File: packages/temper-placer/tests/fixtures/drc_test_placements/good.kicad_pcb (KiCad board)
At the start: 2 copper layers, 50 x 30 mm, 4 parts, among them U1 LM358

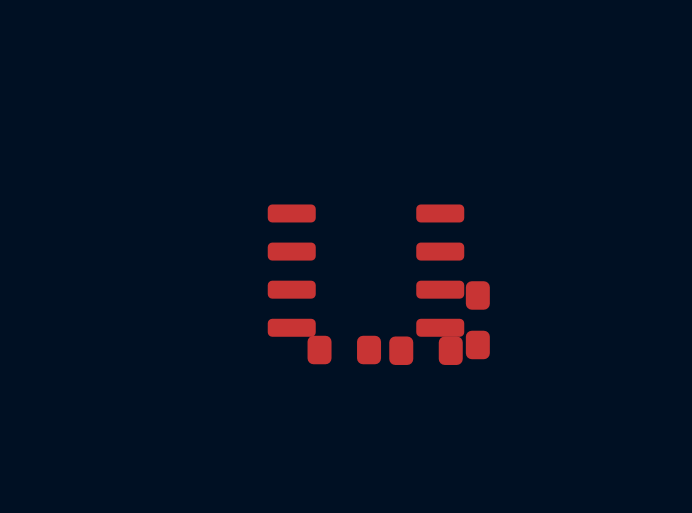
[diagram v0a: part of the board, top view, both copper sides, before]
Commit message: feat(placer): NSGA-II, Crawler, NetCentroidLoss, and structural refinements
- Implemented NSGA-II multi-objective optimization
- Added PcbCrawler for GitHub data collection
- Implemented NetCentroidAttractionLoss
- Unified optimization pipeline with explicit phases
- Fixed ruff linting errors and optimized imports
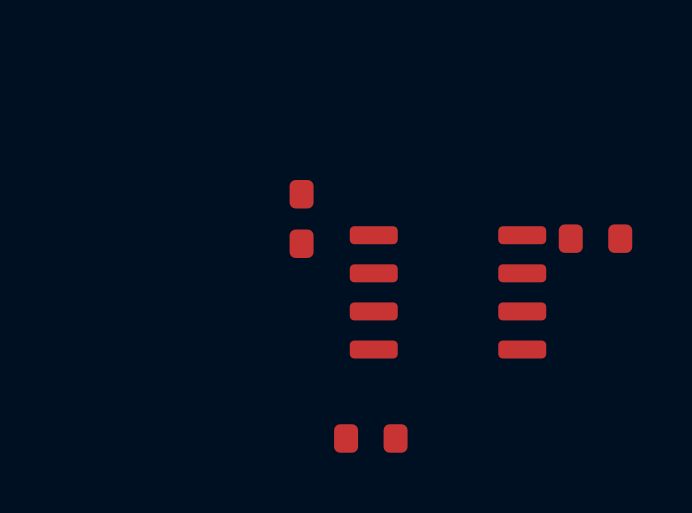
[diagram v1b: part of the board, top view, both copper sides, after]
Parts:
- moved C1 4.77 mm to (212.0, 151.6), turned to 0 degrees
- moved R1 4.59 mm to (202.2, 151.0), turned to 90 degrees
- moved R2 3.46 mm to (204.5, 158.3), turned to 0 degrees
- moved U1 2.83 mm to (207.1, 153.4), turned to 0 degrees
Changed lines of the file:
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@@
   (net 4 "SIG2")
   (footprint "Resistor_SMD:R_0603_1608Metric" (layer "F.Cu")
-    (at 203.62545238394125 155.3403145720717 0.0)
+    (at 202.20253642997244 150.9729914997215 90.0)
     (property "Reference" "R1")
     (property "Value" "10k")
@@
   )
   (footprint "Resistor_SMD:R_0603_1608Metric" (layer "F.Cu")
-    (at 206.34986399963225 155.36405016889017 180.0)
+    (at 204.51042163898182 158.2889805962489 0.0)
     (property "Reference" "R2")
     (property "Value" "4.7k")
@@
   )
   (footprint "Capacitor_SMD:C_0603_1608Metric" (layer "F.Cu")
-    (at 208.07757608066288 154.34710723176667 90.0)
+    (at 211.99947175406612 151.6278695582765 0.0)
     (property "Reference" "C1")
     (property "Value" "100nF")
@@
   )
   (footprint "Package_SO:SOIC-8_3.9x4.9mm_P1.27mm" (layer "F.Cu")
-    (at 204.34950811745597 152.69385059944486 180.0)
+    (at 207.08303911998922 153.41879931193108 0.0)
     (property "Reference" "U1")
     (property "Value" "LM358")

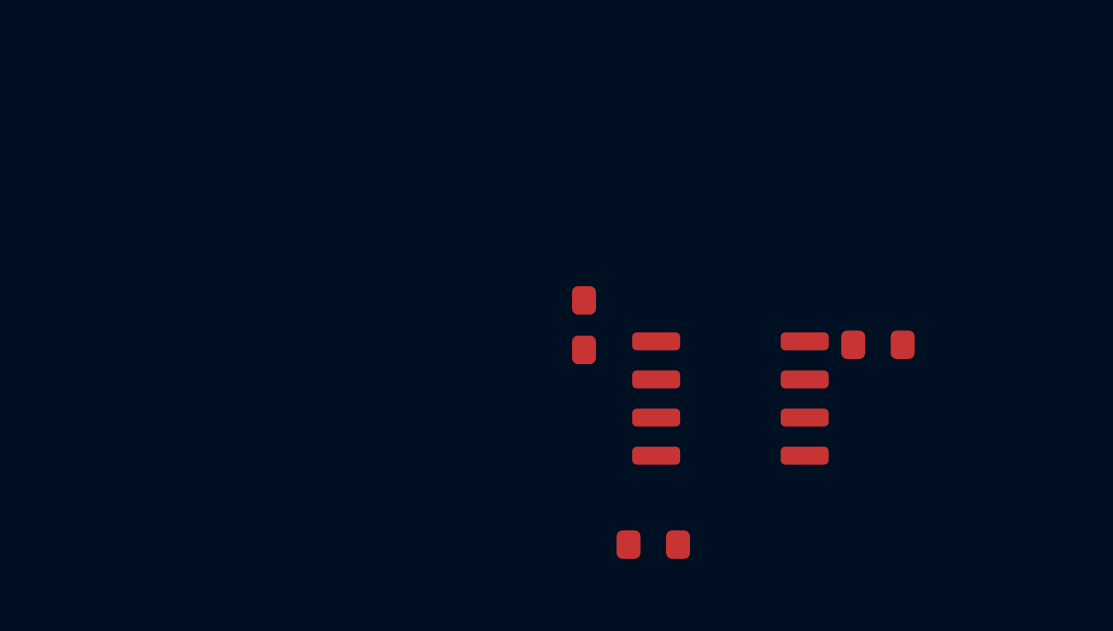
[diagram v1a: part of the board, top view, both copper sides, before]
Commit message: feat(placer): vectorize GroundCrossingLoss and add star-ground awareness
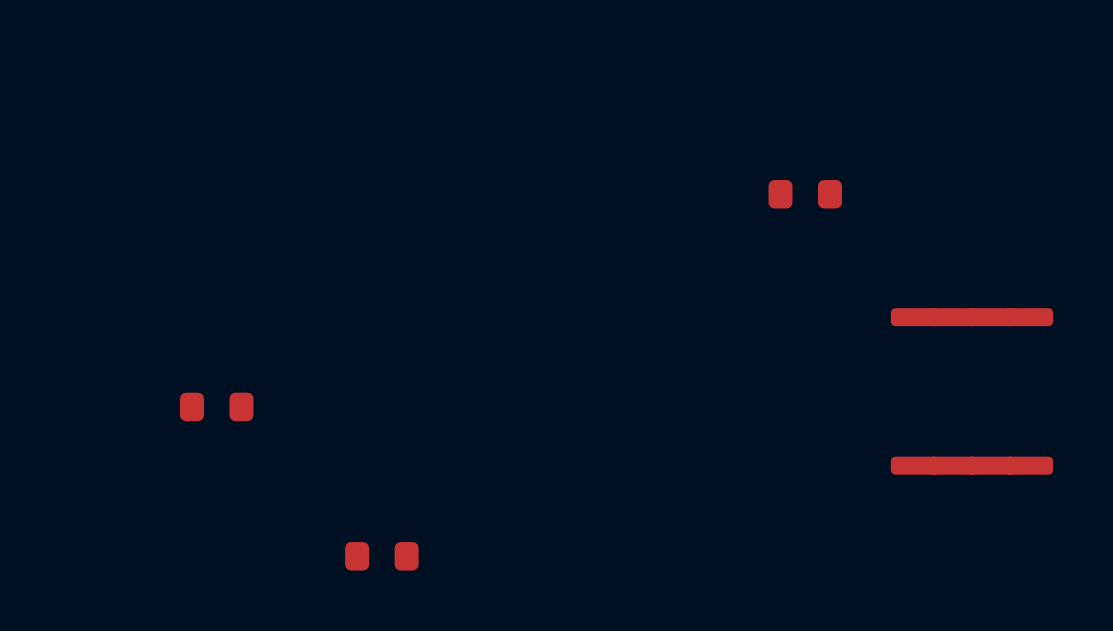
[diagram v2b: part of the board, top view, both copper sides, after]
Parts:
- moved R1 12.5 mm to (190.0, 153.7), turned to 180 degrees
- moved R2 9.05 mm to (195.5, 158.7), turned to 180 degrees
- moved U1 8.06 mm to (215.1, 153.2), turned to 90 degrees
- moved C1 5.57 mm to (209.6, 146.6), turned to 180 degrees
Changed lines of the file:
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@@
   (net 4 "SIG2")
   (footprint "Resistor_SMD:R_0603_1608Metric" (layer "F.Cu")
-    (at 202.20253642997244 150.9729914997215 90.0)
+    (at 189.96026317155744 153.70019848975193 180.0)
     (property "Reference" "R1")
     (property "Value" "10k")
@@
   )
   (footprint "Resistor_SMD:R_0603_1608Metric" (layer "F.Cu")
-    (at 204.51042163898182 158.2889805962489 0.0)
+    (at 195.4638047716711 158.67849316057936 180.0)
     (property "Reference" "R2")
     (property "Value" "4.7k")
@@
   )
   (footprint "Capacitor_SMD:C_0603_1608Metric" (layer "F.Cu")
-    (at 211.99947175406612 151.6278695582765 0.0)
+    (at 209.57740181160239 146.6107337484442 180.0)
     (property "Reference" "C1")
     (property "Value" "100nF")
@@
   )
   (footprint "Package_SO:SOIC-8_3.9x4.9mm_P1.27mm" (layer "F.Cu")
-    (at 207.08303911998922 153.41879931193108 0.0)
+    (at 215.13573126750356 153.18306676152255 90.0)
     (property "Reference" "U1")
     (property "Value" "LM358")

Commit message: feat: Consolidate implementations for Manufacturing, Star Point, and Analysis tasks
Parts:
- turned C1 to 270 degrees
- turned R1 to 270 degrees
- turned R2 to 270 degrees
- turned U1 to 270 degrees
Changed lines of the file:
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@@
   (net 4 "SIG2")
   (footprint "Resistor_SMD:R_0603_1608Metric" (layer "F.Cu")
-    (at 189.96026317155744 153.70019848975193 180.0)
+    (at 189.96026317155744 153.70019848975193 270.0)
     (property "Reference" "R1")
     (property "Value" "10k")
@@
   )
   (footprint "Resistor_SMD:R_0603_1608Metric" (layer "F.Cu")
-    (at 195.4638047716711 158.67849316057936 180.0)
+    (at 195.4638047716711 158.67849316057936 270.0)
     (property "Reference" "R2")
     (property "Value" "4.7k")
@@
   )
   (footprint "Capacitor_SMD:C_0603_1608Metric" (layer "F.Cu")
-    (at 209.57740181160239 146.6107337484442 180.0)
+    (at 209.57740181160239 146.6107337484442 270.0)
     (property "Reference" "C1")
     (property "Value" "100nF")
@@
   )
   (footprint "Package_SO:SOIC-8_3.9x4.9mm_P1.27mm" (layer "F.Cu")
-    (at 215.13573126750356 153.18306676152255 90.0)
+    (at 215.13573126750356 153.18306676152255 270.0)
     (property "Reference" "U1")
     (property "Value" "LM358")

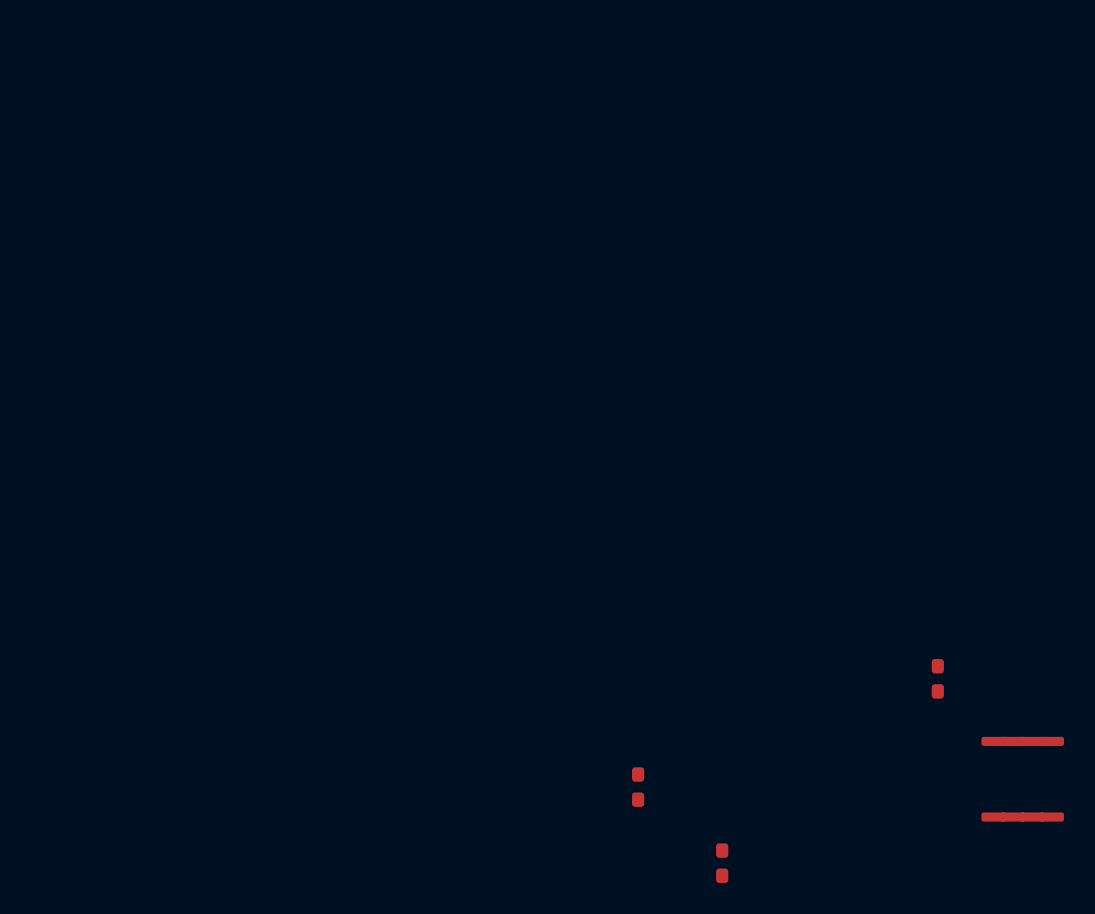
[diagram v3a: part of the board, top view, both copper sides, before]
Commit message: fix(placer): resolve all critical optimizer bugs in temper-p11g
- Fixed JAX array len() TypeErrors by using .shape[0]\n- Corrected BoundaryLoss to use absolute coordinates for non-zero origin boards\n- Implemented hard position and virtual node clamping in training loop\n- Fixed TypeError in force_directed.py random_init call\n- Cleaned up outdated Board/Component signatures in tests
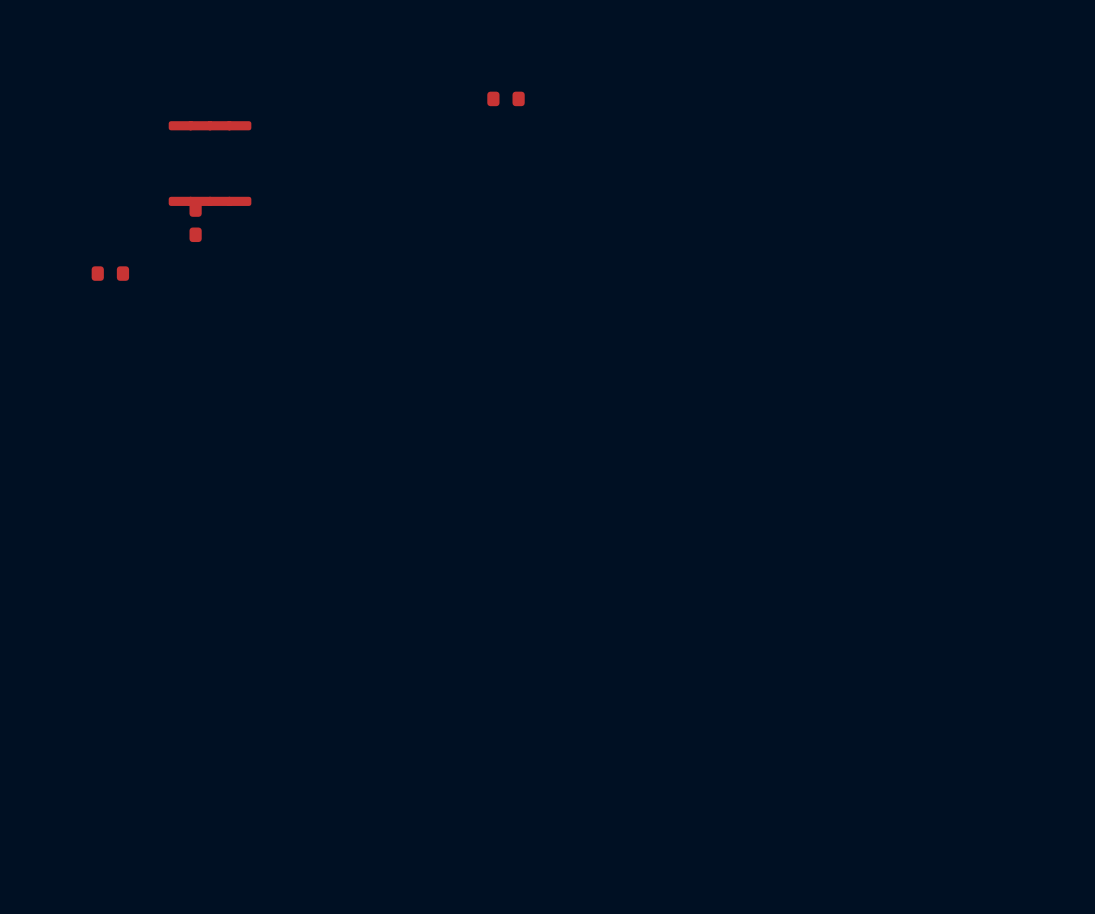
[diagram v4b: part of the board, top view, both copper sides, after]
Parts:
- moved U1 66.7 mm to (161.9, 112.9)
- moved R2 54.3 mm to (161.0, 116.7), turned to 90 degrees
- moved R1 48.2 mm to (155.4, 120.1), turned to 180 degrees
- moved C1 47.3 mm to (181.3, 108.7), turned to 0 degrees
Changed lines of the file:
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@@
   (net 4 "SIG2")
   (footprint "Resistor_SMD:R_0603_1608Metric" (layer "F.Cu")
-    (at 189.96026317155744 153.70019848975193 270.0)
+    (at 155.41230672692365 120.08329051513866 180.0)
     (property "Reference" "R1")
     (property "Value" "10k")
@@
   )
   (footprint "Resistor_SMD:R_0603_1608Metric" (layer "F.Cu")
-    (at 195.4638047716711 158.67849316057936 270.0)
+    (at 160.99183216974504 116.71895349326667 90.0)
     (property "Reference" "R2")
     (property "Value" "4.7k")
@@
   )
   (footprint "Capacitor_SMD:C_0603_1608Metric" (layer "F.Cu")
-    (at 209.57740181160239 146.6107337484442 270.0)
+    (at 181.3108780610052 108.65010905005963 0.0)
     (property "Reference" "C1")
     (property "Value" "100nF")
@@
   )
   (footprint "Package_SO:SOIC-8_3.9x4.9mm_P1.27mm" (layer "F.Cu")
-    (at 215.13573126750356 153.18306676152255 270.0)
+    (at 161.93588563994751 112.88269360655428 270.0)
     (property "Reference" "U1")
     (property "Value" "LM358")
